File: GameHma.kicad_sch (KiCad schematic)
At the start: 0 parts

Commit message: add symbol ESP32 DEVKIT V1 and A4988 STEPPER MOTOR
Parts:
- added U1: ESP32-DEVKIT-V1, ESP32-DEVKIT-V1:MODULE_ESP32_DEVKIT_V1, symbol ESP32-DEVKIT-V1:ESP32-DEVKIT-V1
- added U2: A4988_STEPPER_MOTOR_DRIVER_CARRIER, A4988_STEPPER_MOTOR_DRIVER_CARRIER:MODULE_A4988_STEPPER_MOTOR_DRIVER_CARRIER, symbol A4988_STEPPER_MOTOR_DRIVER_CARRIER:A4988_STEPPER_MOTOR_DRIVER_CARRIER
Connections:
- new net: U2.15 (GND), U2.9 (GND)
- new net: U1.2 (GND), U1.29 (GND)

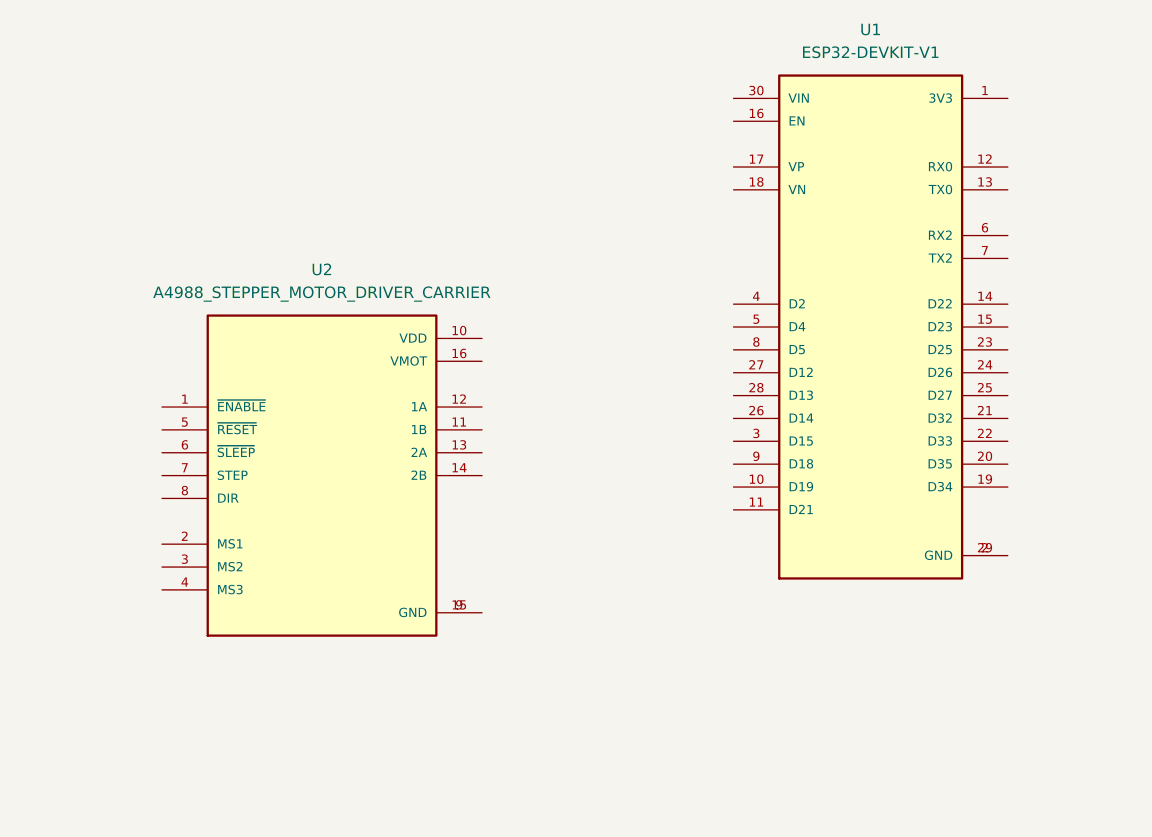
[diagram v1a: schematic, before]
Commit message: connect 3V3 and GND pin
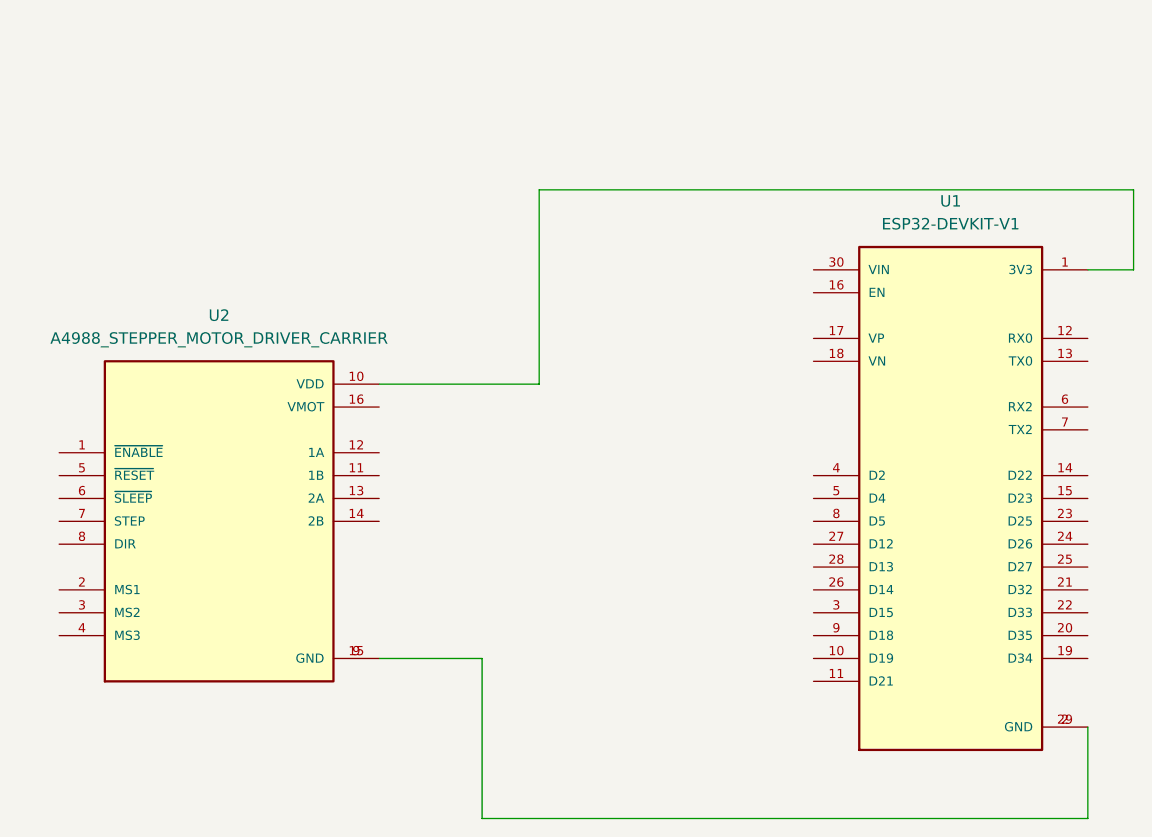
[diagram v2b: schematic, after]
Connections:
- net at U2.10 (VDD): now also U1.1 (3V3)
- net at U2.15 (GND), U2.9 (GND): now also U1.2 (GND), U1.29 (GND)
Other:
- moved on the sheet: U1, U2
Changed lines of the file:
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@@
 		(rev "0")
 	)
+	(wire
+		(pts
+			(xy 177.8 135.89) (xy 110.49 135.89)
+		)
+		(stroke
+			(width 0)
+			(type default)
+		)
+	)
+	(wire
+		(pts
+			(xy 182.88 74.93) (xy 182.88 66.04)
+		)
+		(stroke
+			(width 0)
+			(type default)
+		)
+	)
+	(wire
+		(pts
+			(xy 110.49 118.11) (xy 99.06 118.11)
+		)
+		(stroke
+			(width 0)
+			(type default)
+		)
+	)
+	(wire
+		(pts
+			(xy 116.84 87.63) (xy 99.06 87.63)
+		)
+		(stroke
+			(width 0)
+			(type default)
+		)
+	)
+	(wire
+		(pts
+			(xy 177.8 74.93) (xy 182.88 74.93)
+		)
+		(stroke
+			(width 0)
+			(type default)
+		)
+	)
+	(wire
+		(pts
+			(xy 177.8 125.73) (xy 177.8 135.89)
+		)
+		(stroke
+			(width 0)
+			(type default)
+		)
+	)
+	(wire
+		(pts
+			(xy 182.88 66.04) (xy 116.84 66.04)
+		)
+		(stroke
+			(width 0)
+			(type default)
+		)
+	)
+	(wire
+		(pts
+			(xy 110.49 135.89) (xy 110.49 118.11)
+		)
+		(stroke
+			(width 0)
+			(type default)
+		)
+	)
+	(wire
+		(pts
+			(xy 116.84 66.04) (xy 116.84 87.63)
+		)
+		(stroke
+			(width 0)
+			(type default)
+		)
+	)
 	(image
 		(at 276.86 173.99)
@@
 	(symbol
 		(lib_id "A4988_STEPPER_MOTOR_DRIVER_CARRIER:A4988_STEPPER_MOTOR_DRIVER_CARRIER")
-		(at 92.71 97.79 0)
+		(at 81.28 102.87 0)
 		(unit 1)
 		(exclude_from_sim no)
@@
 		(fields_autoplaced yes)
 		(property "Reference" "U2"
-			(at 92.71 74.93 0)
+			(at 81.28 80.01 0)
 			(effects
 				(font
@@
 		)
 		(property "Value" "A4988_STEPPER_MOTOR_DRIVER_CARRIER"
-			(at 92.71 77.47 0)
+			(at 81.28 82.55 0)
 			(effects
 				(font
@@
 		)
 		(property "Footprint" "A4988_STEPPER_MOTOR_DRIVER_CARRIER:MODULE_A4988_STEPPER_MOTOR_DRIVER_CARRIER"
-			(at 92.71 97.79 0)
+			(at 81.28 102.87 0)
 			(effects
 				(font
@@
 		)
 		(property "Datasheet" ""
-			(at 92.71 97.79 0)
+			(at 81.28 102.87 0)
 			(effects
 				(font
@@
 		)
 		(property "Description" ""
-			(at 92.71 97.79 0)
+			(at 81.28 102.87 0)
 			(effects
 				(font
@@
 		)
 		(property "MF" "Pololu"
-			(at 92.71 97.79 0)
+			(at 81.28 102.87 0)
 			(effects
 				(font
@@
 		)
 		(property "DESCRIPTION" "Stepper motor controler; IC: A4988; 1A; Uin mot: 8÷35V"
-			(at 92.71 97.79 0)
+			(at 81.28 102.87 0)
 			(effects
 				(font
@@
 		)
 		(property "PACKAGE" "None"
-			(at 92.71 97.79 0)
+			(at 81.28 102.87 0)
 			(effects
 				(font
@@
 		)
 		(property "PRICE" "None"
-			(at 92.71 97.79 0)
+			(at 81.28 102.87 0)
 			(effects
 				(font
@@
 		)
 		(property "Package" "None"
-			(at 92.71 97.79 0)
+			(at 81.28 102.87 0)
 			(effects
 				(font
@@
 		)
 		(property "Check_prices" "https://www.snapeda.com/parts/A4988%20STEPPER%20MOTOR%20DRIVER%20CARRIER/Pololu/view-part/?ref=eda"
-			(at 92.71 97.79 0)
+			(at 81.28 102.87 0)
 			(effects
 				(font
@@
 		)
 		(property "Price" "None"
-			(at 92.71 97.79 0)
+			(at 81.28 102.87 0)
 			(effects
 				(font
@@
 		)
 		(property "SnapEDA_Link" "https://www.snapeda.com/parts/A4988%20STEPPER%20MOTOR%20DRIVER%20CARRIER/Pololu/view-part/?ref=snap"
-			(at 92.71 97.79 0)
+			(at 81.28 102.87 0)
 			(effects
 				(font
@@
 		)
 		(property "MP" "A4988 STEPPER MOTOR DRIVER CARRIER"
-			(at 92.71 97.79 0)
+			(at 81.28 102.87 0)
 			(effects
 				(font
@@
 		)
 		(property "Availability" "Not in stock"
-			(at 92.71 97.79 0)
+			(at 81.28 102.87 0)
 			(effects
 				(font
@@
 		)
 		(property "AVAILABILITY" "Unavailable"
-			(at 92.71 97.79 0)
+			(at 81.28 102.87 0)
 			(effects
 				(font
@@
 		)
 		(property "Description_1" "Stepper Motor Driver"
-			(at 92.71 97.79 0)
+			(at 81.28 102.87 0)
 			(effects
 				(font
@@
 	(symbol
 		(lib_id "ESP32-DEVKIT-V1:ESP32-DEVKIT-V1")
-		(at 153.67 81.28 0)
+		(at 162.56 100.33 0)
 		(unit 1)
 		(exclude_from_sim no)
@@
 		(fields_autoplaced yes)
 		(property "Reference" "U1"
-			(at 153.67 48.26 0)
+			(at 162.56 67.31 0)
 			(effects
 				(font
@@
 		)
 		(property "Value" "ESP32-DEVKIT-V1"
-			(at 153.67 50.8 0)
+			(at 162.56 69.85 0)
 			(effects
 				(font
@@
 		)
 		(property "Footprint" "ESP32-DEVKIT-V1:MODULE_ESP32_DEVKIT_V1"
-			(at 153.67 81.28 0)
+			(at 162.56 100.33 0)
 			(effects
 				(font
@@
 		)
 		(property "Datasheet" ""
-			(at 153.67 81.28 0)
+			(at 162.56 100.33 0)
 			(effects
 				(font
@@
 		)
 		(property "Description" ""
-			(at 153.67 81.28 0)
+			(at 162.56 100.33 0)
 			(effects
 				(font
@@
 		)
 		(property "MF" "Do it"
-			(at 153.67 81.28 0)
+			(at 162.56 100.33 0)
 			(effects
 				(font
@@
 		)
 		(property "MAXIMUM_PACKAGE_HEIGHT" "6.8 mm"
-			(at 153.67 81.28 0)
+			(at 162.56 100.33 0)
 			(effects
 				(font
@@
 		)
 		(property "Package" "None"
-			(at 153.67 81.28 0)
+			(at 162.56 100.33 0)
 			(effects
 				(font
@@
 		)
 		(property "Price" "None"
-			(at 153.67 81.28 0)
+			(at 162.56 100.33 0)
 			(effects
 				(font
@@
 		)
 		(property "Check_prices" "https://www.snapeda.com/parts/ESP32-DEVKIT-V1/Do+it/view-part/?ref=eda"
-			(at 153.67 81.28 0)
+			(at 162.56 100.33 0)
 			(effects
 				(font
@@
 		)
 		(property "STANDARD" "Manufacturer Recommendations"
-			(at 153.67 81.28 0)
+			(at 162.56 100.33 0)
 			(effects
 				(font
@@
 		)
 		(property "PARTREV" "N/A"
-			(at 153.67 81.28 0)
+			(at 162.56 100.33 0)
 			(effects
 				(font
@@
 		)
 		(property "SnapEDA_Link" "https://www.snapeda.com/parts/ESP32-DEVKIT-V1/Do+it/view-part/?ref=snap"
-			(at 153.67 81.28 0)
+			(at 162.56 100.33 0)
 			(effects
 				(font
@@
 		)
 		(property "MP" "ESP32-DEVKIT-V1"
-			(at 153.67 81.28 0)
+			(at 162.56 100.33 0)
 			(effects
 				(font
@@
 		)
 		(property "Description_1" "Dual core, Wi-Fi: 2.4 GHz up to 150 Mbits/s,BLE (Bluetooth Low Energy) and legacy Bluetooth, 32 bits, Up to 240 MHz"
-			(at 153.67 81.28 0)
+			(at 162.56 100.33 0)
 			(effects
 				(font
@@
 		)
 		(property "Availability" "Not in stock"
-			(at 153.67 81.28 0)
+			(at 162.56 100.33 0)
 			(effects
 				(font
@@
 		)
 		(property "MANUFACTURER" "DOIT"
-			(at 153.67 81.28 0)
+			(at 162.56 100.33 0)
 			(effects
 				(font

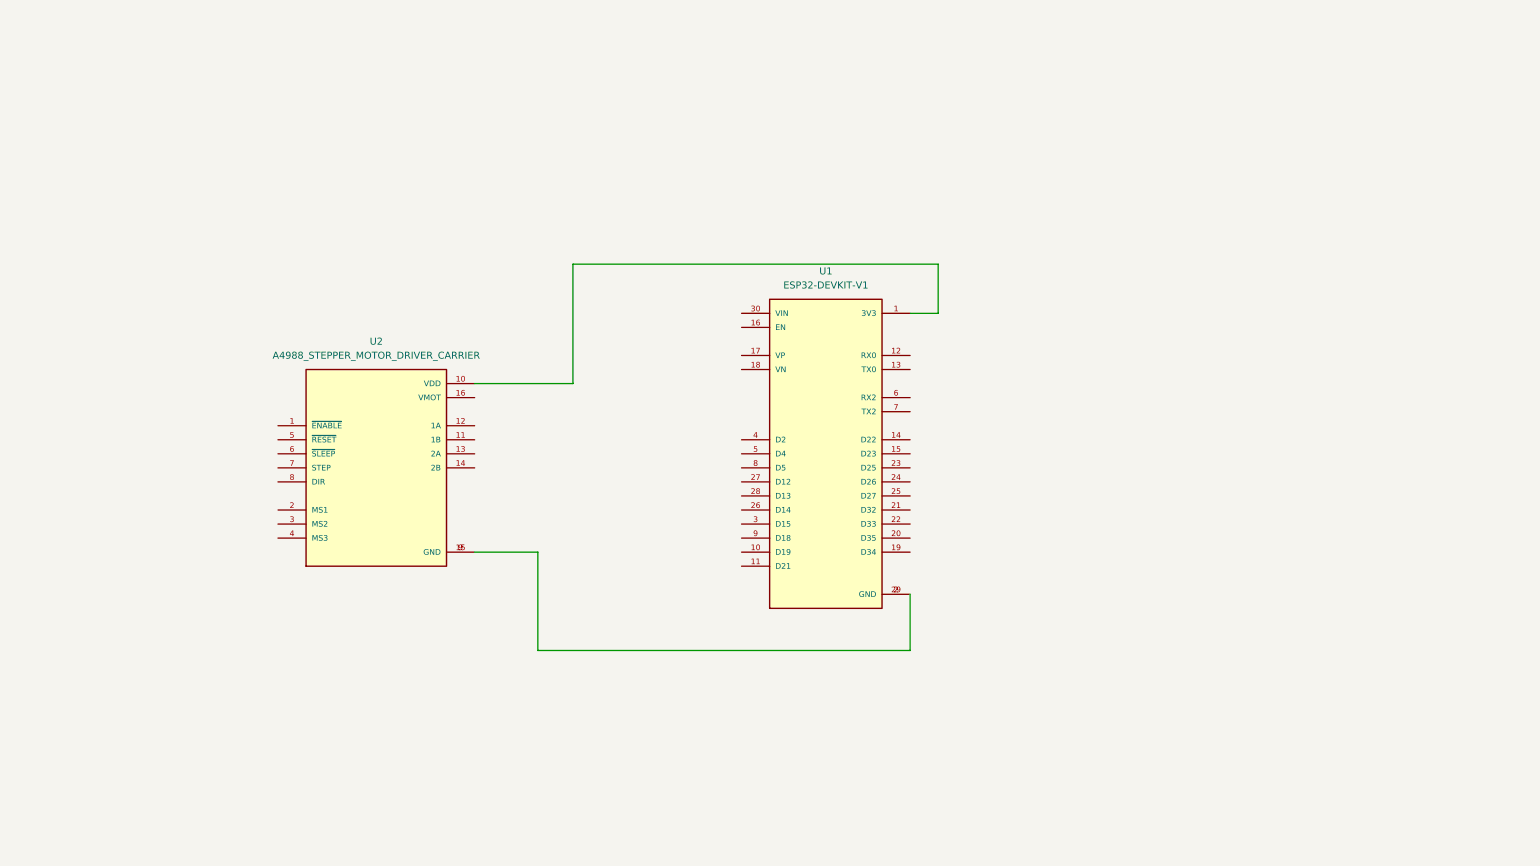
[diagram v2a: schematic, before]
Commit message: add more 3 steper motor, connect 3V3 and GND pins
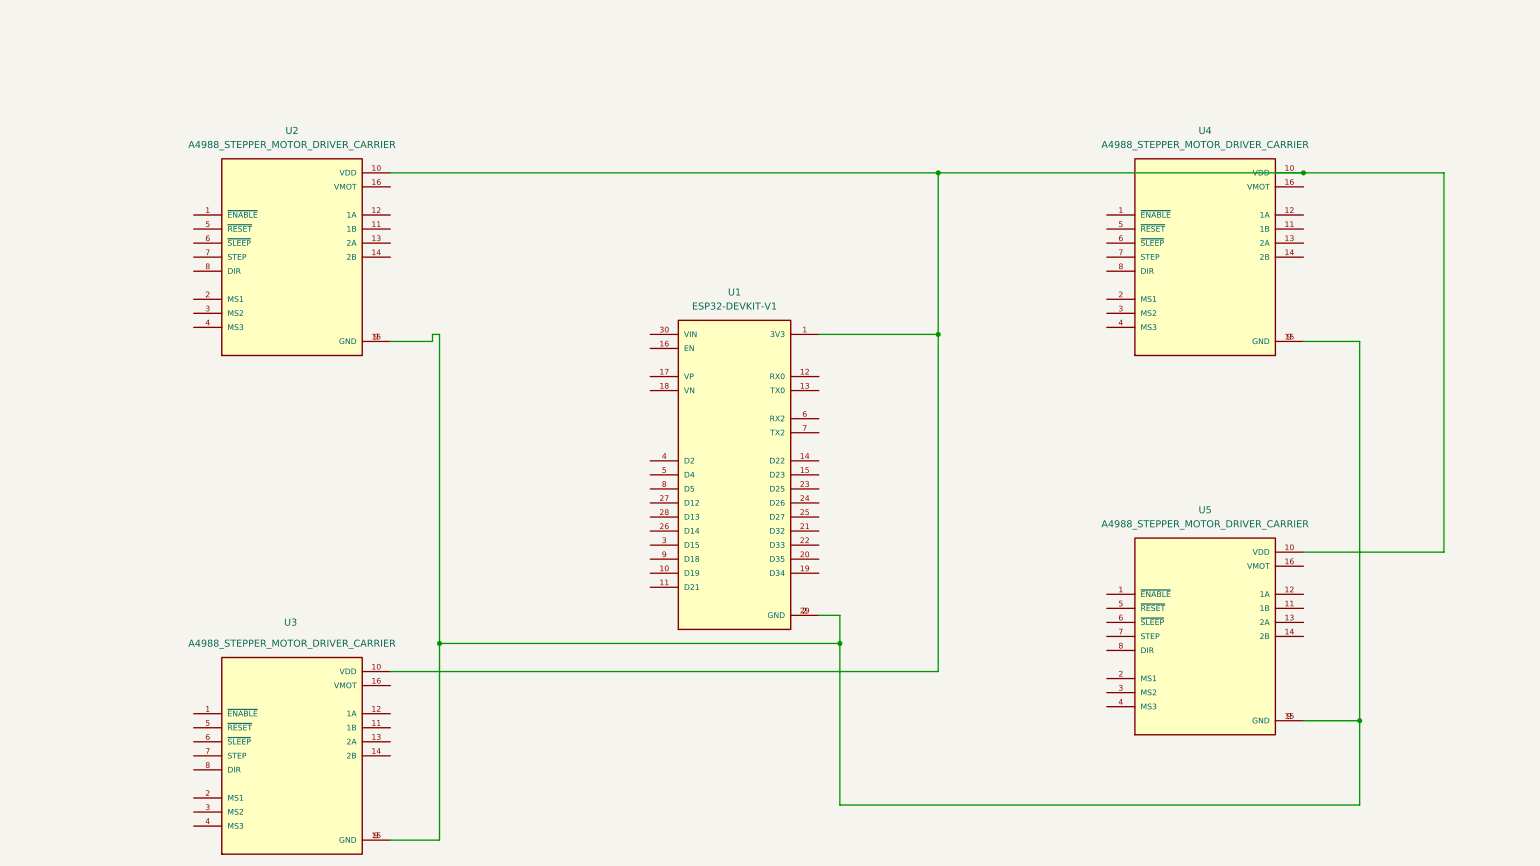
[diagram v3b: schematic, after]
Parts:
- added U3, U4, U5: A4988_STEPPER_MOTOR_DRIVER_CARRIER, A4988_STEPPER_MOTOR_DRIVER_CARRIER:MODULE_A4988_STEPPER_MOTOR_DRIVER_CARRIER, symbol A4988_STEPPER_MOTOR_DRIVER_CARRIER:A4988_STEPPER_MOTOR_DRIVER_CARRIER
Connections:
- net at U1.1 (3V3), U2.10 (VDD): now also U3.10 (VDD), U4.10 (VDD), U5.10 (VDD)
- net at U1.2 (GND), U1.29 (GND), U2.15 (GND)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: now also U3.15 (GND), U3.9 (GND), U4.15 (GND), U4.9 (GND), U5.15 (GND), U5.9 (GND)
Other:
- moved on the sheet: U1, U2

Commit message: add Battery terminal and Motor terminal, connect Vin and edit VMOT in U4 because it wrong connetion
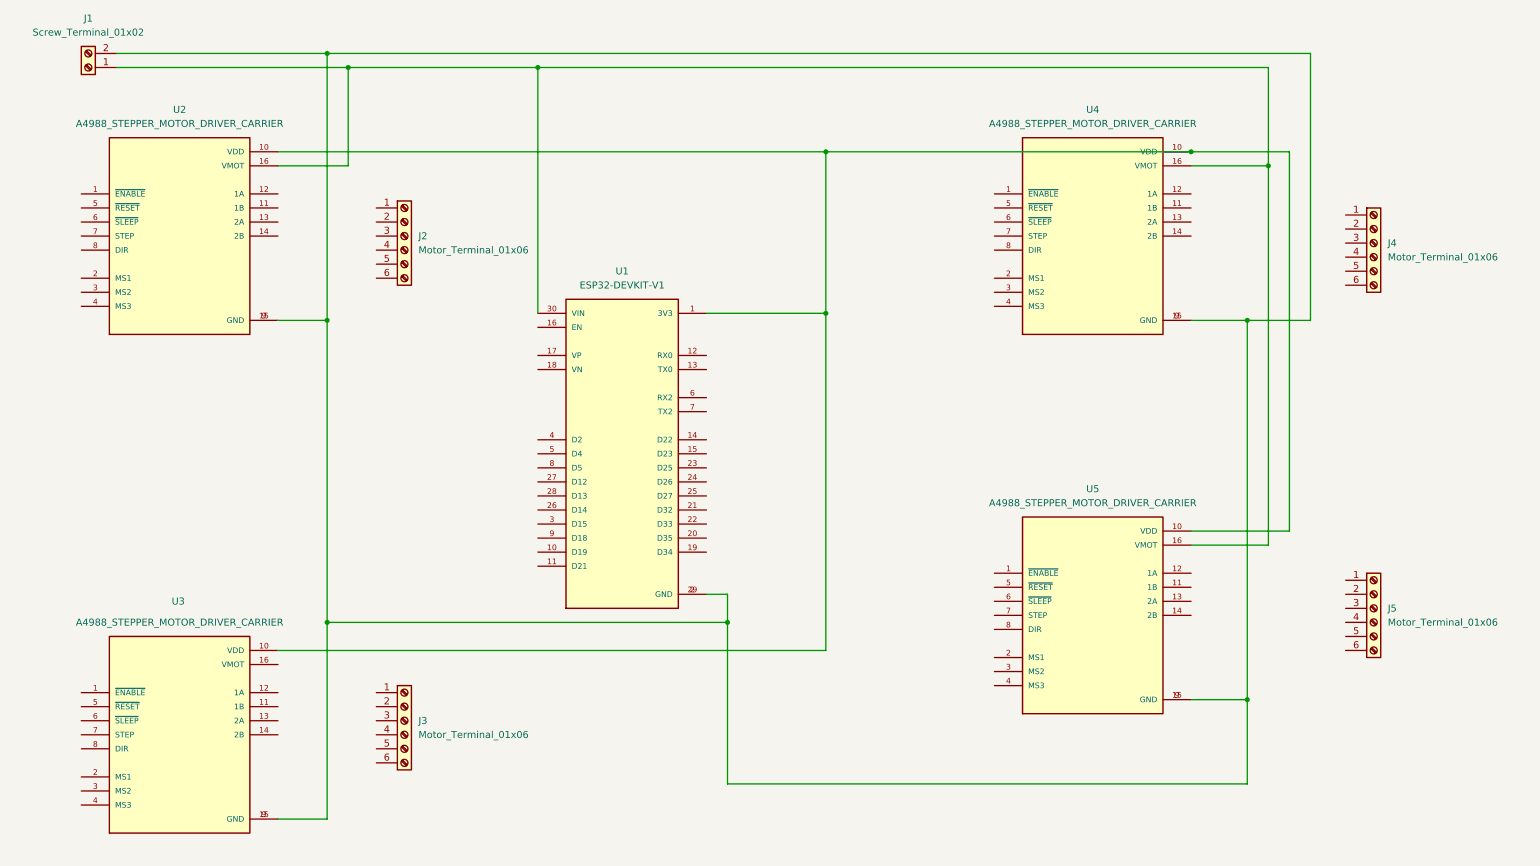
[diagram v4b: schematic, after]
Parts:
- added J1: Screw_Terminal_01x02, symbol Connector:Screw_Terminal_01x02
- added J2, J3, J4, J5: Motor_Terminal_01x06, symbol Connector:Screw_Terminal_01x06
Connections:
- net at U1.2 (GND), U1.29 (GND), U2.15 (GND)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: now also J1.2 (Pin_2)
- net at U2.16 (VMOT): now also U1.30 (VIN), U4.16 (VMOT), U5.16 (VMOT), J1.1 (Pin_1)
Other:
- moved on the sheet: U1, U2, U3, U4, U5
